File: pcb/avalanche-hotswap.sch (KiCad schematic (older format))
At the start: 138 parts, among them J1 TRRS, J2 LED, J3 OLED, P1 i2c_pin, P2 i2c_pin, SW1 SW_Push, SW10 SW_Push, SW11 SW_Push, SW12 SW_Push, SW13 SW_Push, SW14 SW_Push, SW15 SW_Push, SW16 SW_Push, SW17 SW_Push, SW18 SW_Push, SW19 SW_Push, SW2 SW_Push, SW20 SW_Push, SW21 SW_Push, SW22 SW_Push, SW23 SW_Push, SW24 SW_Push, SW25 SW_Push, SW26 SW_Push, SW27 SW_Push, SW28 SW_Push, SW29 SW_Push, SW3 SW_Push, SW30 SW_Push, SW31 SW_Push, SW32 SW_Push, SW4 SW_Push, SW5 SW_Push, SW6 SW_Push, SW7 SW_Push, SW8 SW_Push, SW9 SW_Push, U1 ProMicro

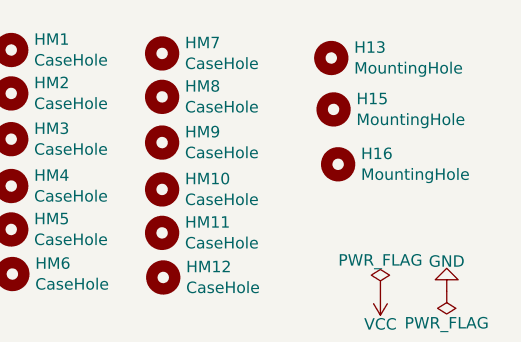
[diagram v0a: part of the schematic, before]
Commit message: Routed RESET in its new location.
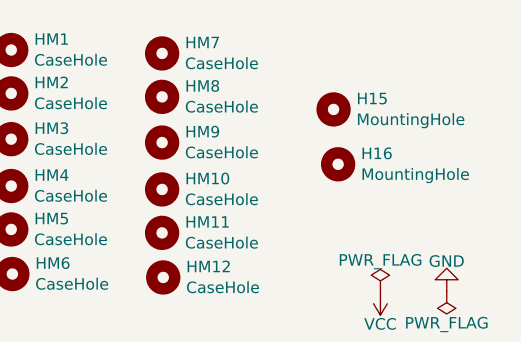
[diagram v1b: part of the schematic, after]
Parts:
- removed H13: MountingHole, used_footprints:M2_HOLE_PCB, symbol Mechanical:MountingHole
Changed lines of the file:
@@
 	1560 3015 2050 3015
-$Comp
-L Mechanical:MountingHole H13
-U 1 1 605332C5
-P 10330 690
-F 0 "H13" H 10430 736 50  0000 L CNN
-F 1 "MountingHole" H 10430 645 50  0000 L CNN
-F 2 "used_footprints:M2_HOLE_PCB" H 10330 690 50  0001 C CNN
-F 3 "~" H 10330 690 50  0001 C CNN
-	1    10330 690
-	1    0    0    -1
-$EndComp
 $Comp
 L Mechanical:MountingHole H15

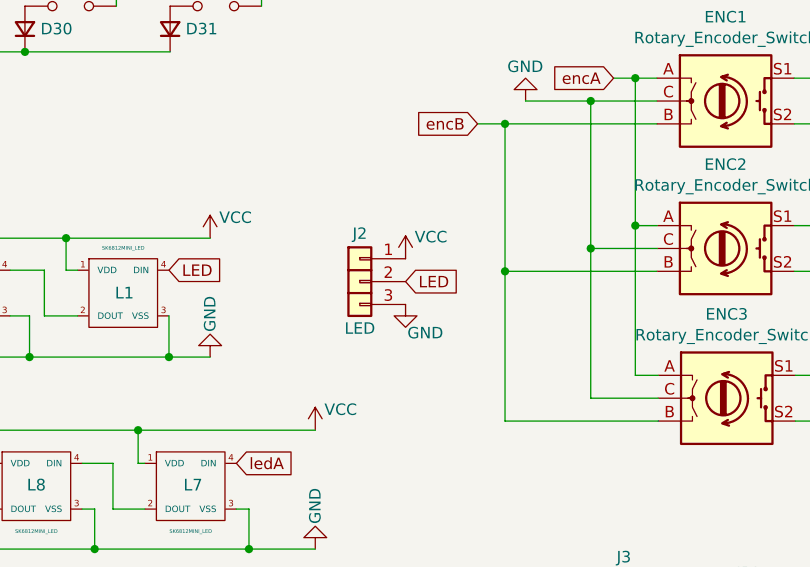
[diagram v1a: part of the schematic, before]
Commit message: New egde cuts
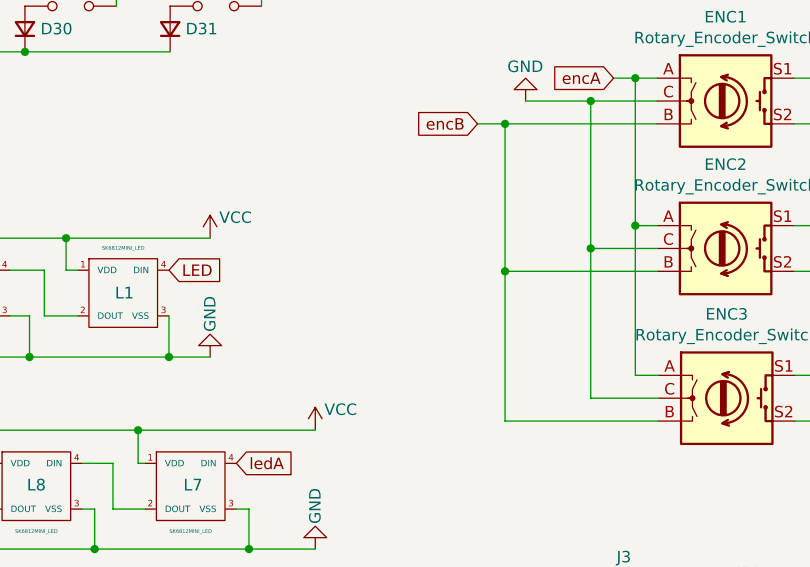
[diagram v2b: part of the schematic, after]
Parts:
- removed J2: LED, used_footprints:LED, symbol avalanche-hotswap:LED
- SW28, SW29: footprint used_footprints:CherryMX_MidHeight_Hotswap_1.25u -> used_footprints:CherryMX_MidHeight_Hotswap_1u
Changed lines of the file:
@@
 F 0 "SW28" H 6145 2645 50  0000 C CNN
 F 1 "SW_Push" H 6145 2684 50  0001 C CNN
-F 2 "used_footprints:CherryMX_MidHeight_Hotswap_1.25u" H 6145 2690 50  0001 C CNN
+F 2 "used_footprints:CherryMX_MidHeight_Hotswap_1u" H 6145 2690 50  0001 C CNN
 F 3 "~" H 6145 2690 50  0001 C CNN
 	1    6145 2490
@@
 F 0 "SW29" H 6745 2645 50  0000 C CNN
 F 1 "SW_Push" H 6745 2684 50  0001 C CNN
-F 2 "used_footprints:CherryMX_MidHeight_Hotswap_1.25u" H 6745 2690 50  0001 C CNN
+F 2 "used_footprints:CherryMX_MidHeight_Hotswap_1u" H 6745 2690 50  0001 C CNN
 F 3 "~" H 6745 2690 50  0001 C CNN
 	1    6745 2490
@@
 Text GLabel 2745 3015 2    50   Input ~ 0
 DATA
-$Comp
-L avalanche-hotswap:LED J2
-U 1 1 605D77A0
-P 8620 3695
-F 0 "J2" H 8620 3905 50  0000 C CNN
-F 1 "LED" H 8620 3490 50  0000 C CNN
-F 2 "used_footprints:LED" H 8620 3695 50  0001 C CNN
-F 3 "" H 8620 3695 50  0001 C CNN
-	1    8620 3695
-	1    0    0    -1
-$EndComp
-$Comp
-L power:VCC #PWR0105
-U 1 1 605DF8D6
-P 8820 3595
-F 0 "#PWR0105" H 8820 3445 50  0001 C CNN
-F 1 "VCC" H 8860 3690 50  0000 L CNN
-F 2 "" H 8820 3595 50  0001 C CNN
-F 3 "" H 8820 3595 50  0001 C CNN
-	1    8820 3595
-	1    0    0    -1
-$EndComp
-Text GLabel 8820 3695 2    50   Input ~ 0
-LED
-$Comp
-L power:GND #PWR0106
-U 1 1 605E60EC
-P 8820 3795
-F 0 "#PWR0106" H 8820 3545 50  0001 C CNN
-F 1 "GND" H 8985 3670 50  0000 R CNN
-F 2 "" H 8820 3795 50  0001 C CNN
-F 3 "" H 8820 3795 50  0001 C CNN
-	1    8820 3795
-	1    0    0    -1
-$EndComp
 Text GLabel 2585 1140 2    50   Input ~ 0
 RST

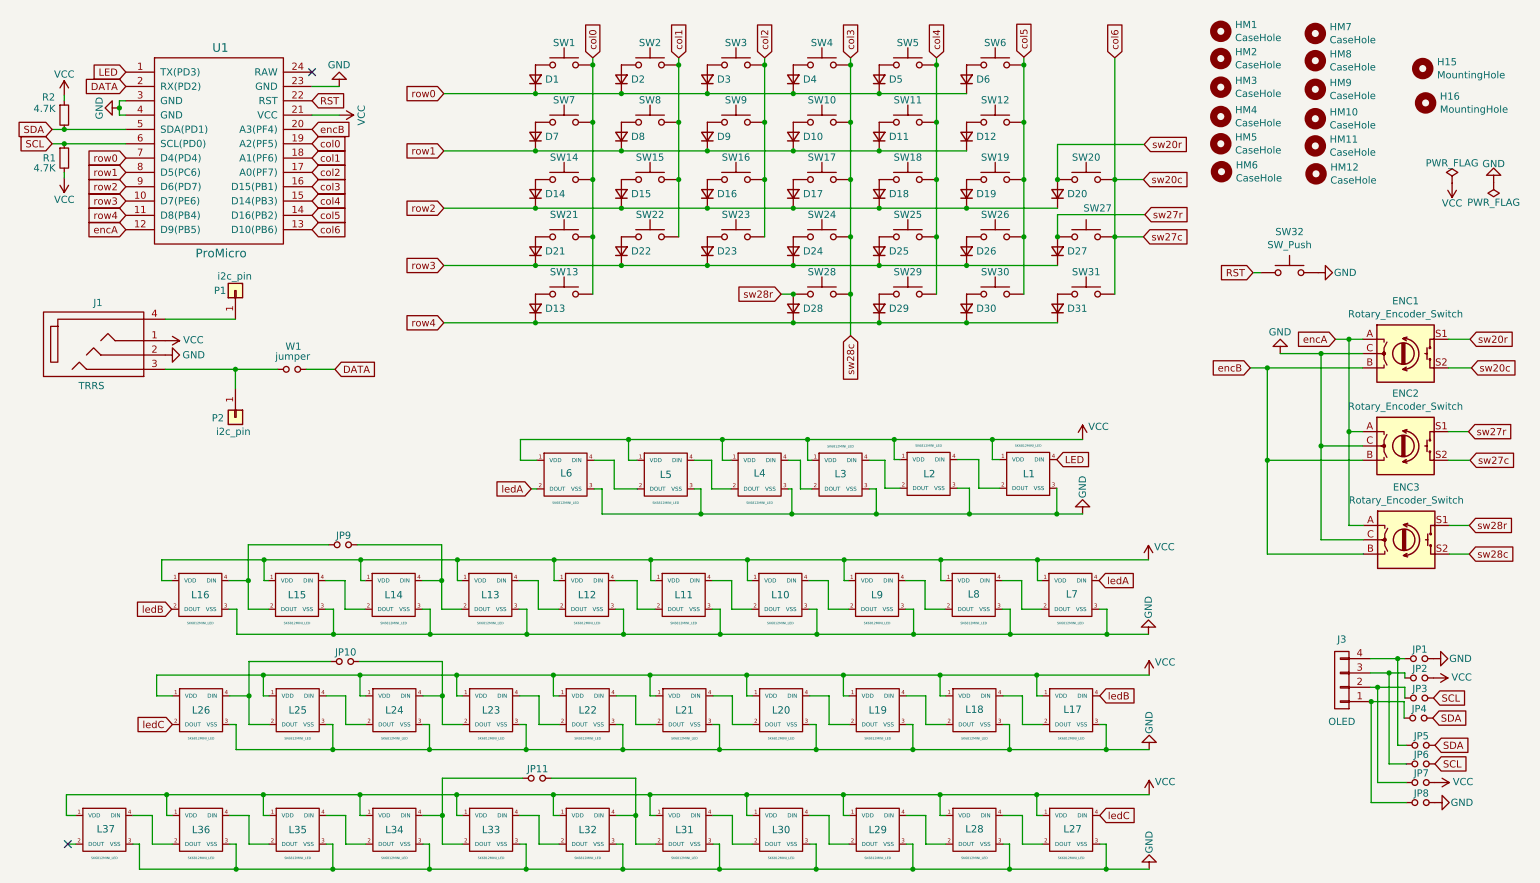
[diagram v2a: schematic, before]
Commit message: Added one more button!
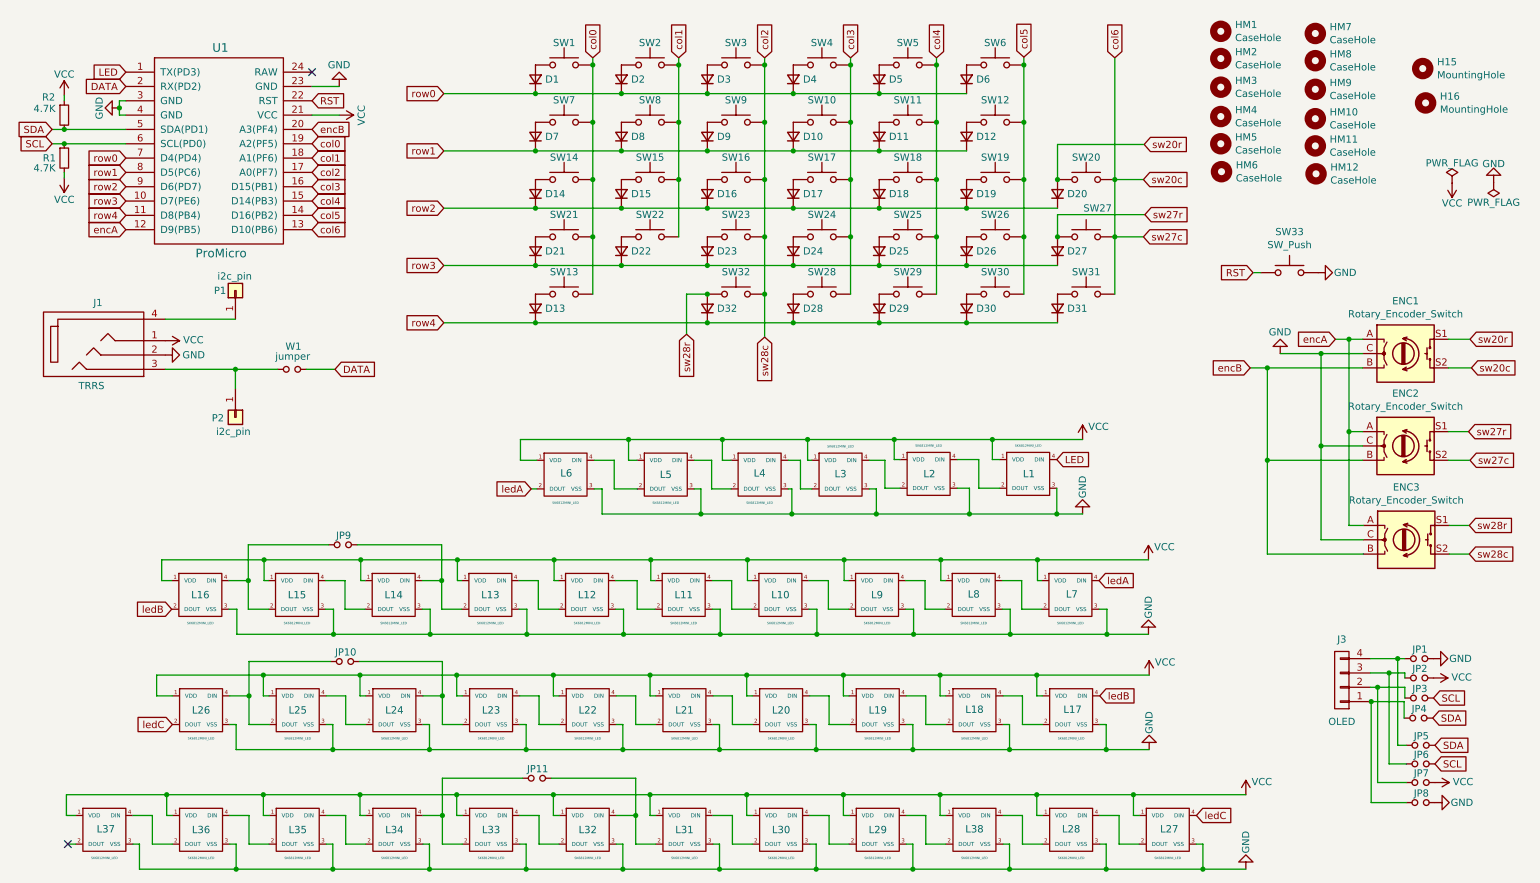
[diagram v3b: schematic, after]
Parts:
- added D32: 1N4148, used_footprints:diode_TH_SMD, symbol Device:D_Small
- added L38: SK6812MINI_LED, used_footprints:YS-SK6812MINI-E, symbol avalanche-hotswap:SK6812MINI_LED
- added SW32: SW_Push, used_footprints:CherryMX_MidHeight_Hotswap_1u, symbol Switch:SW_Push
- renumbered SW32 to SW33
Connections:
- net GND: now also L38.3 (VSS)
- net VCC: now also L38.1 (VDD)
- net col2: now also ENC3.S2, SW32.2
- net col3: no longer ENC3.S2
- net row4: now also D32.1 (K)
- net sw28r: now also D32.2 (A), SW32.1; no longer D28.2 (A), SW28.1
- net at L29.4 (DIN): now also L38.2 (DOUT); no longer L28.2 (DOUT)
- new net: D28.2 (A), SW28.1
- new net: L28.2 (DOUT), L38.4 (DIN)
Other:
- moved on the sheet: L27, L28
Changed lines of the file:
@@
 	6945 890  6945 1290
-$Comp
-L Switch:SW_Push SW32
-U 1 1 5DBF73FF
-P 9410 2340
-F 0 "SW32" H 9410 2625 50  0000 C CNN
-F 1 "SW_Push" H 9410 2534 50  0000 C CNN
-F 2 "used_footprints:Switch_Reset_THT" H 9410 2540 50  0001 C CNN
-F 3 "~" H 9410 2540 50  0001 C CNN
-	1    9410 2340
-	1    0    0    -1
-$EndComp
 $Comp
 L power:GND #PWR08
@@
 	4545 2090 4545 2490
 Connection ~ 4545 2090
-Text GLabel 5860 2490 0    50   Input ~ 0
-sw28r
-Text GLabel 6345 2780 3    50   Input ~ 0
-sw28c
-Wire Wire Line
-	6345 2490 6345 2780
-Connection ~ 6345 2490
 Text GLabel 8395 1445 2    50   Input ~ 0
 sw20r
@@
 $EndComp
 Wire Wire Line
-	4145 2690 5945 2690
-Wire Wire Line
 	5945 2690 6545 2690
 Connection ~ 5945 2690
-Wire Wire Line
-	5860 2490 5945 2490
-Connection ~ 5945 2490
 Wire Wire Line
 	7790 2090 7790 1935
@@
 $EndComp
 $Comp
-L avalanche-hotswap:SK6812MINI_LED L28
-U 1 1 614A7669
-P 7210 6230
-F 0 "L28" H 7210 6235 51  0000 C CNN
-F 1 "SK6812MINI_LED" H 7210 6033 16  0000 C CNN
-F 2 "used_footprints:YS-SK6812MINI-E" H 7210 6230 60  0001 C CNN
-F 3 "" H 7210 6230 60  0001 C CNN
-	1    7210 6230
-	1    0    0    -1
-$EndComp
-$Comp
 L avalanche-hotswap:SK6812MINI_LED L29
 U 1 1 614A7684
@@
 $EndComp
 $Comp
-L power:VCC #PWR0114
-U 1 1 614A769D
-P 8430 5985
-F 0 "#PWR0114" H 8430 5835 50  0001 C CNN
-F 1 "VCC" H 8470 6075 50  0000 L CNN
-F 2 "" H 8430 5985 50  0001 C CNN
-F 3 "" H 8430 5985 50  0001 C CNN
-	1    8430 5985
-	1    0    0    -1
-$EndComp
-$Comp
-L power:GND #PWR0115
-U 1 1 614A76A3
-P 8430 6505
-F 0 "#PWR0115" H 8430 6255 50  0001 C CNN
-F 1 "GND" V 8430 6395 50  0000 R CNN
-F 2 "" H 8430 6505 50  0001 C CNN
-F 3 "" H 8430 6505 50  0001 C CNN
-	1    8430 6505
-	-1   0    0    1
-$EndComp
-$Comp
 L avalanche-hotswap:SK6812MINI_LED L30
 U 1 1 614A76A9
@@
 Text GLabel 1605 4690 0    50   Input ~ 0
 ledB
-Text GLabel 1610 5495 0    50   Input ~ 0
-ledC
-Text GLabel 8085 6130 2    50   Input ~ 0
-ledC
 NoConn ~ 880  6330
 $Comp
@@
 $EndComp
 $Comp
-L avalanche-hotswap:SK6812MINI_LED L27
-U 1 1 614A766F
-P 7885 6230
-F 0 "L27" H 7895 6235 51  0000 C CNN
-F 1 "SK6812MINI_LED" H 7885 6033 16  0000 C CNN
-F 2 "used_footprints:YS-SK6812MINI-E" H 7885 6230 60  0001 C CNN
-F 3 "" H 7885 6230 60  0001 C CNN
-	1    7885 6230
-	1    0    0    -1
-$EndComp
-$Comp
 L avalanche-hotswap:SK6812MINI_LED L37
 U 1 1 614E2B97
@@
 	2055 5495 2055 5670
 Wire Wire Line
-	2055 5670 2730 5670
-Wire Wire Line
 	7010 5295 6970 5295
 Wire Wire Line
@@
 	2245 5150 2920 5150
 Wire Wire Line
-	7685 6130 7645 6130
-Wire Wire Line
-	7645 6130 7645 5985
-Connection ~ 7645 5985
-Wire Wire Line
-	7645 5985 8430 5985
-Wire Wire Line
-	7010 6130 6970 6130
-Wire Wire Line
-	6970 6130 6970 5985
-Connection ~ 6970 5985
-Wire Wire Line
-	6970 5985 7645 5985
-Wire Wire Line
 	6335 6130 6295 6130
 Wire Wire Line
 	6295 6130 6295 5985
-Connection ~ 6295 5985
-Wire Wire Line
-	6295 5985 6970 5985
 Wire Wire Line
 	5660 6130 5620 6130
@@
 Connection ~ 5620 5985
 Wire Wire Line
-	5620 5985 6295 5985
-Wire Wire Line
 	4985 6130 4945 6130
 Wire Wire Line
@@
 	1570 6130 1570 5985
 Wire Wire Line
-	8085 6330 8130 6330
-Wire Wire Line
-	8130 6330 8130 6505
-Connection ~ 8130 6505
-Wire Wire Line
-	8130 6505 8430 6505
-Wire Wire Line
-	7410 6330 7455 6330
-Wire Wire Line
-	7455 6330 7455 6505
-Connection ~ 7455 6505
-Wire Wire Line
-	7455 6505 8130 6505
-Wire Wire Line
 	6735 6330 6780 6330
 Wire Wire Line
 	6780 6330 6780 6505
-Connection ~ 6780 6505
-Wire Wire Line
-	6780 6505 7455 6505
 Wire Wire Line
 	6060 6330 6105 6330
@@
 Connection ~ 6105 6505
 Wire Wire Line
-	6105 6505 6780 6505
-Wire Wire Line
 	5385 6330 5430 6330
 Wire Wire Line
@@
 	2145 5495 2145 5295
 Wire Wire Line
-	7685 6330 7545 6330
-Wire Wire Line
-	7545 6330 7545 6130
-Wire Wire Line
-	7545 6130 7410 6130
-Wire Wire Line
-	7010 6330 6870 6330
-Wire Wire Line
-	6870 6330 6870 6130
-Wire Wire Line
-	6870 6130 6735 6130
-Wire Wire Line
 	6335 6330 6195 6330
 Wire Wire Line
@@
 	4855 4490 4705 4490
 Wire Wire Line
-	2245 5150 1500 5150
-Wire Wire Line
-	1500 5150 1500 5295
-Wire Wire Line
 	1500 5295 1610 5295
 Connection ~ 2245 5150
+Wire Wire Line
+	2055 5670 2730 5670
+Text GLabel 1610 5495 0    50   Input ~ 0
+ledC
+$Comp
+L Switch:SW_Push SW33
+U 1 1 5DBF73FF
+P 9410 2340
+F 0 "SW33" H 9410 2625 50  0000 C CNN
+F 1 "SW_Push" H 9410 2534 50  0000 C CNN
+F 2 "used_footprints:Switch_Reset_THT" H 9410 2540 50  0001 C CNN
+F 3 "~" H 9410 2540 50  0001 C CNN
+	1    9410 2340
+	1    0    0    -1
+$EndComp
+$Comp
+L Device:D_Small D32
+U 1 1 609231D8
+P 5345 2590
+F 0 "D32" V 5345 2522 50  0000 R CNN
+F 1 "1N4148" V 5300 2522 50  0001 R CNN
+F 2 "used_footprints:diode_TH_SMD" V 5345 2590 50  0001 C CNN
+F 3 "~" V 5345 2590 50  0001 C CNN
+	1    5345 2590
+	0    -1   -1   0
+$EndComp
+$Comp
+L Switch:SW_Push SW32
+U 1 1 609231DE
+P 5545 2490
+F 0 "SW32" H 5545 2645 50  0000 C CNN
+F 1 "SW_Push" H 5545 2684 50  0001 C CNN
+F 2 "used_footprints:CherryMX_MidHeight_Hotswap_1u" H 5545 2690 50  0001 C CNN
+F 3 "~" H 5545 2690 50  0001 C CNN
+	1    5545 2490
+	1    0    0    -1
+$EndComp
+Wire Wire Line
+	4145 2690 5345 2690
+Wire Wire Line
+	5345 2690 5945 2690
+Connection ~ 5345 2690
+Connection ~ 5745 2090
+Wire Wire Line
+	5200 2490 5345 2490
+Connection ~ 5345 2490
+Text GLabel 5200 2770 3    50   Input ~ 0
+sw28r
+Wire Wire Line
+	5200 2490 5200 2770
+Wire Wire Line
+	2245 5150 1500 5150
+Wire Wire Line
+	1500 5150 1500 5295
+Text GLabel 5745 2790 3    50   Input ~ 0
+sw28c
+Wire Wire Line
+	5745 2090 5745 2490
+Wire Wire Line
+	5745 2490 5745 2790
+Connection ~ 5745 2490
+Wire Wire Line
+	6105 6505 6780 6505
+Wire Wire Line
+	5620 5985 6295 5985
+Wire Wire Line
+	6970 5985 7645 5985
+Wire Wire Line
+	6870 6130 6735 6130
+Wire Wire Line
+	6870 6330 6870 6130
+Wire Wire Line
+	7010 6330 6870 6330
+Wire Wire Line
+	7455 6330 7455 6505
+Wire Wire Line
+	7410 6330 7455 6330
+Connection ~ 6970 5985
+Wire Wire Line
+	6970 6130 6970 5985
+Wire Wire Line
+	7010 6130 6970 6130
+$Comp
+L avalanche-hotswap:SK6812MINI_LED L38
+U 1 1 60FC11F2
+P 7210 6230
+F 0 "L38" H 7210 6235 51  0000 C CNN
+F 1 "SK6812MINI_LED" H 7210 6033 16  0000 C CNN
+F 2 "used_footprints:YS-SK6812MINI-E" H 7210 6230 60  0001 C CNN
+F 3 "" H 7210 6230 60  0001 C CNN
+	1    7210 6230
+	1    0    0    -1
+$EndComp
+Wire Wire Line
+	7545 6130 7410 6130
+Wire Wire Line
+	7545 6330 7545 6130
+Wire Wire Line
+	7685 6330 7545 6330
+Wire Wire Line
+	8220 6130 8085 6130
+Wire Wire Line
+	8220 6330 8220 6130
+Wire Wire Line
+	8360 6330 8220 6330
+Wire Wire Line
+	8130 6505 8805 6505
+Connection ~ 8130 6505
+Wire Wire Line
+	8130 6330 8130 6505
+Wire Wire Line
+	8085 6330 8130 6330
+Wire Wire Line
+	8805 6505 9105 6505
+Connection ~ 8805 6505
+Wire Wire Line
+	8805 6330 8805 6505
+Wire Wire Line
+	8760 6330 8805 6330
+Wire Wire Line
+	7645 5985 8320 5985
+Connection ~ 7645 5985
+Wire Wire Line
+	7645 6130 7645 5985
+Wire Wire Line
+	7685 6130 7645 6130
+Wire Wire Line
+	8320 5985 9105 5985
+Connection ~ 8320 5985
+Wire Wire Line
+	8320 6130 8320 5985
+Wire Wire Line
+	8360 6130 8320 6130
+$Comp
+L avalanche-hotswap:SK6812MINI_LED L27
+U 1 1 614A766F
+P 8560 6230
+F 0 "L27" H 8570 6235 51  0000 C CNN
+F 1 "SK6812MINI_LED" H 8560 6033 16  0000 C CNN
+F 2 "used_footprints:YS-SK6812MINI-E" H 8560 6230 60  0001 C CNN
+F 3 "" H 8560 6230 60  0001 C CNN
+	1    8560 6230
+	1    0    0    -1
+$EndComp
+Text GLabel 8760 6130 2    50   Input ~ 0
+ledC
+$Comp
+L power:GND #PWR0115
+U 1 1 614A76A3
+P 9105 6505
+F 0 "#PWR0115" H 9105 6255 50  0001 C CNN
+F 1 "GND" V 9105 6395 50  0000 R CNN
+F 2 "" H 9105 6505 50  0001 C CNN
+F 3 "" H 9105 6505 50  0001 C CNN
+	1    9105 6505
+	-1   0    0    1
+$EndComp
+$Comp
+L power:VCC #PWR0114
+U 1 1 614A769D
+P 9105 5985
+F 0 "#PWR0114" H 9105 5835 50  0001 C CNN
+F 1 "VCC" H 9145 6075 50  0000 L CNN
+F 2 "" H 9105 5985 50  0001 C CNN
+F 3 "" H 9105 5985 50  0001 C CNN
+	1    9105 5985
+	1    0    0    -1
+$EndComp
+$Comp
+L avalanche-hotswap:SK6812MINI_LED L28
+U 1 1 614A7669
+P 7885 6230
+F 0 "L28" H 7885 6235 51  0000 C CNN
+F 1 "SK6812MINI_LED" H 7885 6033 16  0000 C CNN
+F 2 "used_footprints:YS-SK6812MINI-E" H 7885 6230 60  0001 C CNN
+F 3 "" H 7885 6230 60  0001 C CNN
+	1    7885 6230
+	1    0    0    -1
+$EndComp
+Wire Wire Line
+	6295 5985 6970 5985
+Connection ~ 6295 5985
+Wire Wire Line
+	6780 6505 7455 6505
+Connection ~ 6780 6505
+Connection ~ 7455 6505
+Wire Wire Line
+	7455 6505 8130 6505
 $EndSCHEMATC
